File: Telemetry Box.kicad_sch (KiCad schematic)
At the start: 0 parts

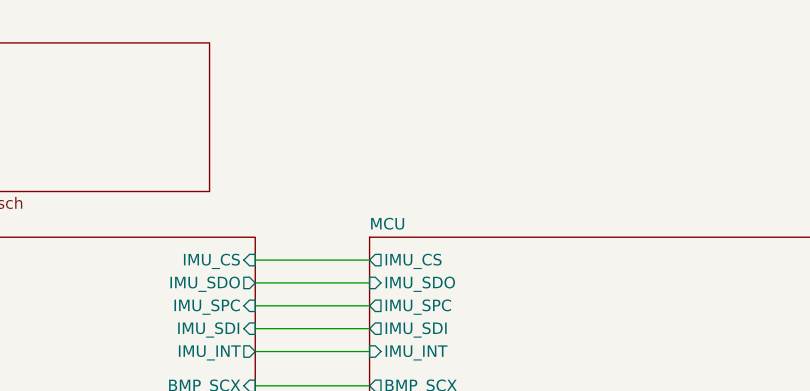
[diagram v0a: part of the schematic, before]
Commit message: Schematics complete; Starting layout. Removed 2 thermistors, not necessary. Going to update website once layout starts
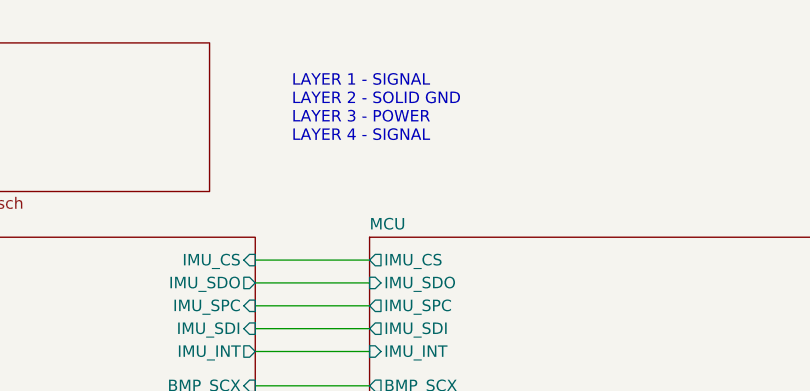
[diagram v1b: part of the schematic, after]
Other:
- note added: "LAYER 1 - SIGNAL LAYER 2 - SOLID GND LAYER 3 - POWER LAYER 4 - SIGNAL"
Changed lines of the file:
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@@
 	(generator_version "10.0")
 	(paper "A4")
+	(text "LAYER 1 - SIGNAL\nLAYER 2 - SOLID GND\nLAYER 3 - POWER\nLAYER 4 - SIGNAL"
+		(exclude_from_sim no)
+		(at 94.234 72.136 0)
+		(effects
+			(font
+				(size 1.27 1.27)
+			)
+			(justify left)
+		)
+	)
 	(wire
 		(pts

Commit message: Final schematic and initial layout
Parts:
- added H1, H2: MountingHole_Pad, MountingHole:MountingHole_3.2mm_M3_DIN965_Pad, symbol Mechanical:MountingHole_Pad
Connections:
- new net PGND: H1.1, H2.1
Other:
- sheet MCU ports: added GPS_RST, GPS_SCL, GPS_SDA, GPS_TP, THERM1, THERM2; removed none
- sheet Sensors ports: added GPS_RST, GPS_SCL, GPS_SDA, GPS_TP, THERM1, THERM2; removed none

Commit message: Finished initial signal layout
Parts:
- H1, H2: footprint MountingHole:MountingHole_3.2mm_M3_DIN965_Pad -> MountingHole:MountingHole_2.2mm_M2_DIN965_Pad
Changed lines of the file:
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@@
 			)
 		)
-		(property "Footprint" "MountingHole:MountingHole_3.2mm_M3_DIN965_Pad"
+		(property "Footprint" "MountingHole:MountingHole_2.2mm_M2_DIN965_Pad"
 			(at 104.14 152.4 0)
 			(hide yes)
@@
 			)
 		)
-		(property "Footprint" "MountingHole:MountingHole_3.2mm_M3_DIN965_Pad"
+		(property "Footprint" "MountingHole:MountingHole_2.2mm_M2_DIN965_Pad"
 			(at 128.27 152.4 0)
 			(hide yes)

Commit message: Updated schematics for rev2
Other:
- sheet Converters ports: added USB_DN, USB_DP; removed none
- sheet MCU ports: added USB_DN, USB_DP; removed none
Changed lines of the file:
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@@
 	(text "LAYER 1 - SIGNAL\nLAYER 2 - SOLID GND\nLAYER 3 - POWER\nLAYER 4 - SIGNAL"
 		(exclude_from_sim no)
-		(at 94.234 72.136 0)
+		(at 77.724 45.974 0)
 		(effects
 			(font
@@
 	(wire
 		(pts
+			(xy 90.17 119.38) (xy 102.87 119.38)
+		)
+		(stroke
+			(width 0)
+			(type default)
+		)
+	)
+	(wire
+		(pts
+			(xy 90.17 110.49) (xy 102.87 110.49)
+		)
+		(stroke
+			(width 0)
+			(type default)
+		)
+	)
+	(wire
+		(pts
+			(xy 104.14 154.94) (xy 104.14 157.48)
+		)
+		(stroke
+			(width 0)
+			(type default)
+		)
+	)
+	(wire
+		(pts
 			(xy 90.17 124.46) (xy 102.87 124.46)
 		)
@@
 	(wire
 		(pts
-			(xy 90.17 119.38) (xy 102.87 119.38)
-		)
-		(stroke
-			(width 0)
-			(type default)
-		)
-	)
-	(wire
-		(pts
-			(xy 90.17 110.49) (xy 102.87 110.49)
-		)
-		(stroke
-			(width 0)
-			(type default)
-		)
-	)
-	(wire
-		(pts
-			(xy 104.14 154.94) (xy 104.14 157.48)
+			(xy 96.52 82.55) (xy 102.87 82.55)
 		)
 		(stroke
@@
 	(wire
 		(pts
+			(xy 86.36 59.69) (xy 99.06 59.69)
+		)
+		(stroke
+			(width 0)
+			(type default)
+		)
+	)
+	(wire
+		(pts
 			(xy 90.17 113.03) (xy 102.87 113.03)
 		)
@@
 	(wire
 		(pts
+			(xy 99.06 59.69) (xy 99.06 80.01)
+		)
+		(stroke
+			(width 0)
+			(type default)
+		)
+	)
+	(wire
+		(pts
+			(xy 99.06 80.01) (xy 102.87 80.01)
+		)
+		(stroke
+			(width 0)
+			(type default)
+		)
+	)
+	(wire
+		(pts
 			(xy 90.17 96.52) (xy 102.87 96.52)
 		)
@@
 	(wire
 		(pts
+			(xy 86.36 62.23) (xy 96.52 62.23)
+		)
+		(stroke
+			(width 0)
+			(type default)
+		)
+	)
+	(wire
+		(pts
 			(xy 90.17 88.9) (xy 102.87 88.9)
 		)
@@
 		(pts
 			(xy 90.17 121.92) (xy 102.87 121.92)
+		)
+		(stroke
+			(width 0)
+			(type default)
+		)
+	)
+	(wire
+		(pts
+			(xy 96.52 62.23) (xy 96.52 82.55)
 		)
 		(stroke
@@
 	)
 	(sheet
-		(at 41.91 86.36)
-		(size 48.26 48.26)
+		(at 41.91 76.2)
+		(size 48.26 58.42)
 		(exclude_from_sim no)
 		(in_bom yes)
@@
 		)
 		(property "Sheetname" "Sensors"
-			(at 41.91 85.6484 0)
+			(at 41.91 75.4884 0)
 			(show_name no)
 			(do_not_autoplace no)
@@
 		)
 		(property "Field2" ""
-			(at 41.91 86.36 0)
+			(at 41.91 76.2 0)
 			(hide yes)
 			(show_name no)
@@
 	)
 	(sheet
-		(at 102.87 86.36)
-		(size 50.8 48.26)
+		(at 102.87 76.2)
+		(size 50.8 58.42)
 		(exclude_from_sim no)
 		(in_bom yes)
@@
 		)
 		(property "Sheetname" "MCU"
-			(at 102.87 85.6484 0)
+			(at 102.87 75.4884 0)
 			(show_name no)
 			(do_not_autoplace no)
@@
 		(pin "GPS_SCL" input
 			(at 102.87 119.38 180)
+			(effects
+				(font
+					(size 1.27 1.27)
+				)
+				(justify left)
+			)
+		)
+		(pin "USB_DN" bidirectional
+			(at 102.87 82.55 180)
+			(effects
+				(font
+					(size 1.27 1.27)
+				)
+				(justify left)
+			)
+		)
+		(pin "USB_DP" bidirectional
+			(at 102.87 80.01 180)
 			(effects
 				(font
@@
 	)
 	(sheet
-		(at 41.91 64.77)
+		(at 43.18 52.07)
 		(size 43.18 16.51)
 		(exclude_from_sim no)
@@
 		)
 		(property "Sheetname" "Converters"
-			(at 41.91 64.0584 0)
+			(at 43.18 51.3584 0)
 			(show_name no)
 			(do_not_autoplace no)
@@
 		)
 		(property "Sheetfile" "converters.kicad_sch"
-			(at 41.91 81.8646 0)
+			(at 43.18 69.1646 0)
 			(show_name no)
 			(do_not_autoplace no)
@@
 		)
 		(property "Field2" ""
-			(at 41.91 64.77 0)
-			(hide yes)
-			(show_name no)
-			(do_not_autoplace no)
-			(effects
-				(font
-					(size 1.27 1.27)
-				)
-			)
-		)
+			(at 43.18 52.07 0)
+			(hide yes)
+			(show_name no)
+			(do_not_autoplace no)
+			(effects
+				(font
+					(size 1.27 1.27)
+				)
+			)
+		)
+		(pin "USB_DN" bidirectional
+			(at 86.36 62.23 0)
+			(effects
+				(font
+					(size 1.27 1.27)
+				)
+				(justify right)
+			)
+		)
+		(pin "USB_DP" bidirectional
+			(at 86.36 59.69 0)
+			(effects
+				(font
+					(size 1.27 1.27)
+				)
+				(justify right)
+			)
+		)
